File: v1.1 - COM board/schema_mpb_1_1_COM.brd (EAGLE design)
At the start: 72.2 x 75.2 mm, 4 parts, among them IC1 E73_2G4M04S, U1 ESP-WROOM-32

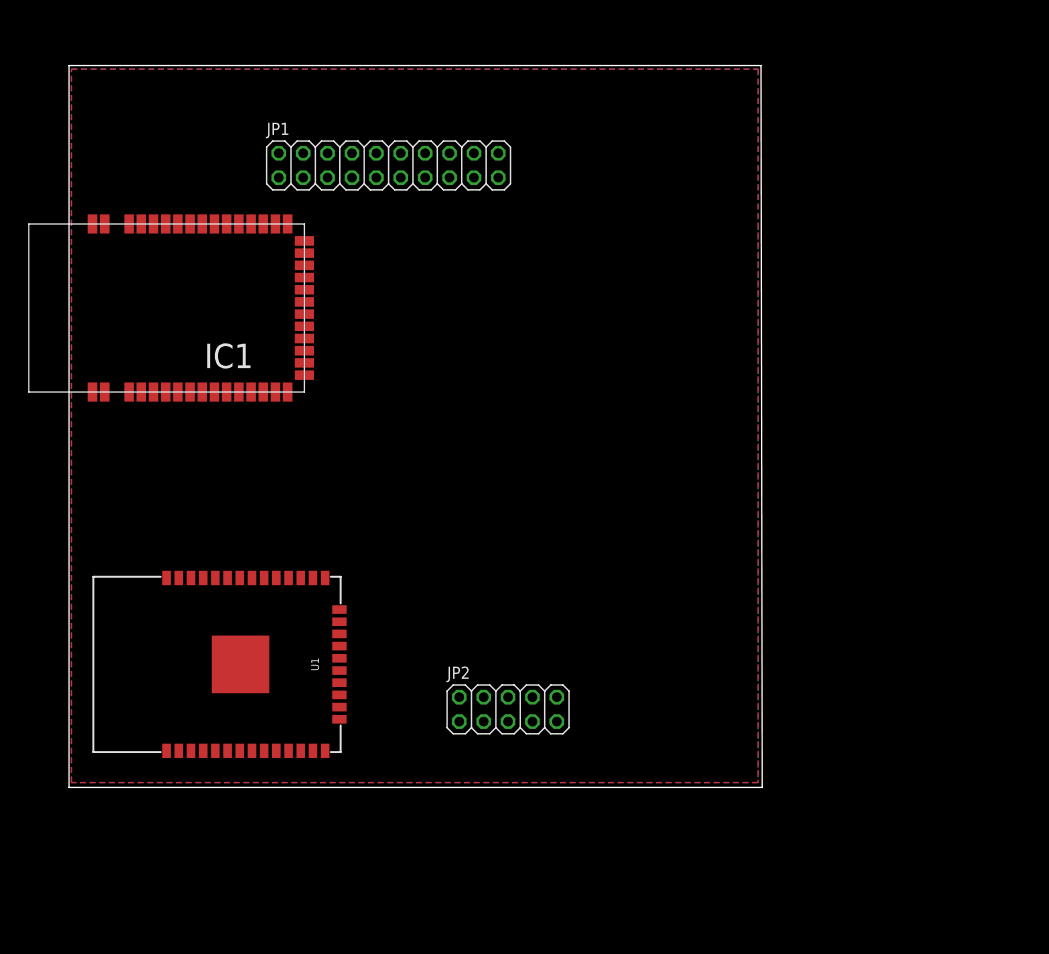
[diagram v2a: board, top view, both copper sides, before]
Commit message: COM board
- Routed first version of Wireless COM board
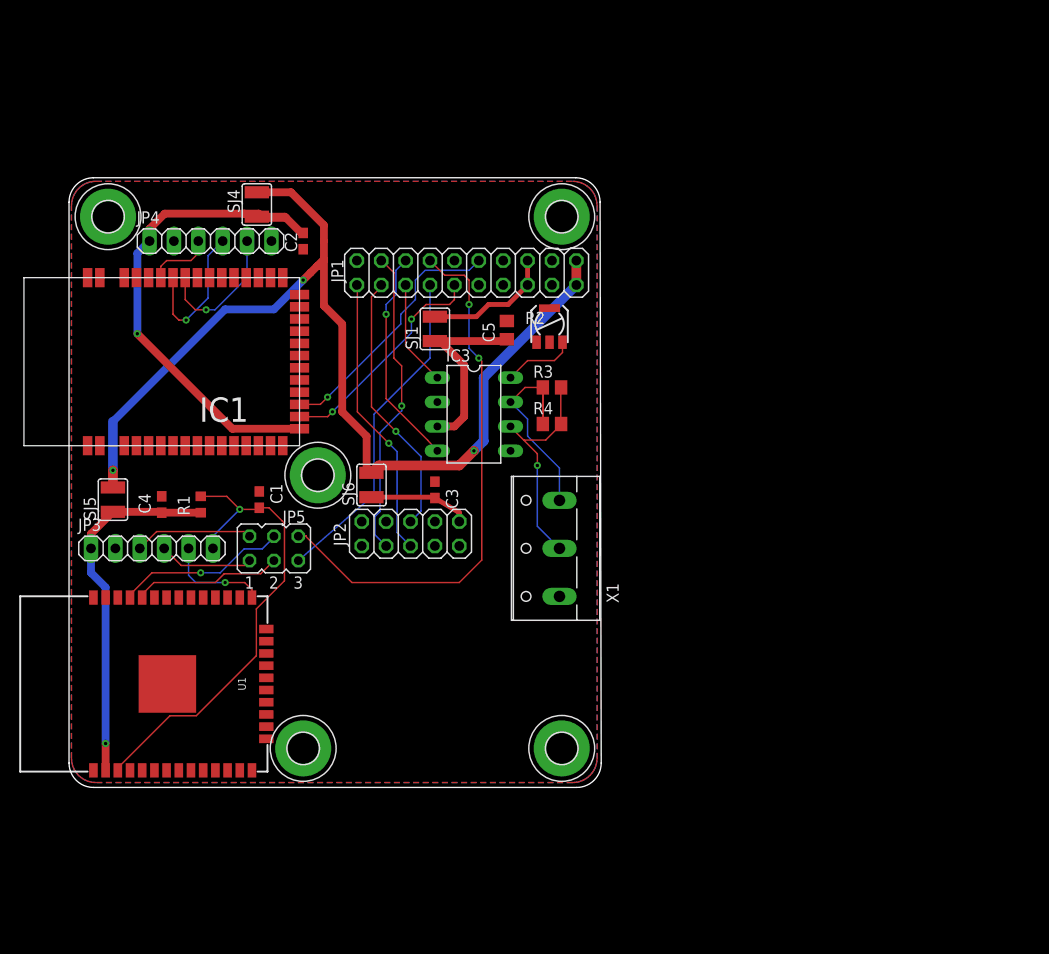
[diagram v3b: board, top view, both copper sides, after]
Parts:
- added C1, C2, C4: .1uF, resistor:C0603
- added C3: (no value), resistor:C0603
- added C5: 0.1uF, resistor:C0805
- added H1, H2, H3, H4, H5: MOUNT-PAD-ROUND3.2, holes:3,2-PAD
- added IC3: PCA82C250, micro-philips:DIL08
- added JP3, JP4: (no value), pinhead:1X06
- added JP5: (no value), jumper:JP3Q
- added R1: 10K, resistor:R0603
- added R2: 25K to 200K, pot-vitrohm:PC25
- added R3, R4: 120, resistor:R0805
- added SJ1, SJ4, SJ5, SJ6: (no value), jumper:SJW
- added X1: (no value), con-wago-500:W237-103
- moved JP2 20.9 mm to (35.6, 26.4), turned to 180 degrees
- moved JP1 13.8 mm to (41.4, 53.6)
- moved U1 7.89 mm to (10.2, 10.8)
- moved IC1 5.61 mm to (24.0, 53.1)
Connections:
- net NRF_IRQ renamed PB8
- net NRF_MISO renamed PB4
- removed net N$10: IC1.36
- removed net N$2: U1.2
- removed net N$3: U1.35
- removed net N$4: U1.34
- removed net N$5: U1.15
- removed net N$6: IC1.0, IC1.1, IC1.15, IC1.2, IC1.42, IC1.43
- removed net N$8: IC1.37
- removed net N$9: IC1.16
- removed net NRF_CE: JP1.9
- removed net NRF_CS: JP1.12
- removed net NRF_MOSI: JP1.7
- removed net NRF_SCK: JP1.8
- new net CANH: IC3.7, R3.2, R4.2, X1.3
- new net CANL: IC3.6, R3.1, R4.1, X1.2
- new net ESP_EN: C1.2, JP3.6, R1.2, U1.3
- new net ESP_IO0: JP3.5, U1.25
- new net ESP_RX: JP1.7, JP5.5
- new net ESP_RX#: JP3.4, JP5.1
- new net ESP_RXD: JP5.3, U1.34
- new net ESP_TX: JP1.8, JP5.6
- new net ESP_TX#: JP3.3, JP5.2
- new net ESP_TXD: JP5.4, U1.35
- new net ETH_CLK: JP2.9
- new net ETH_CS: JP2.3
- new net ETH_NT: JP2.10
- new net ETH_RST: JP2.4
- new net N$12: U1.20
- new net NRF_RST: IC1.36, JP4.5
- new net NRF_RX: IC1.18, JP1.12
- new net NRF_SWDCLK: IC1.37, JP4.4
- new net NRF_SWDIO: IC1.38, JP4.3
- new net NRF_TX: IC1.17, JP1.9
- new net VCC_CAN: C5.1, IC3.3, SJ1.1
- new net VCC_ESP: C4.2, JP3.1, R1.1, SJ5.1, U1.2
- new net VCC_ETH: C3.2, JP2.1, SJ6.1
- new net VCC_NRF: C2.2, IC1.16, JP4.1, SJ4.1
- new net WOL: JP2.7
- net +3.3V: now also SJ4.2, SJ5.2, SJ6.2
- net +5V: now also SJ1.2
- net CAN1_RX: now also IC3.1
- net CAN1_TX: now also IC3.4
- net ETH_MISO: now also JP2.8
- net ETH_MOSI: now also JP2.5
- net ETH_SCK: now also JP2.6
- net GND: now also C1.1, C2.1, C3.1, C4.1, C5.2, IC1.0, IC1.1, IC1.15, IC1.2, IC1.42, IC1.43, IC3.2, JP2.2, JP3.2, JP4.2, R2.A, U1.1, U1.15, U1.38, X1.1
- net N$1: now also IC3.8, R2.E; no longer U1.1
- net N$7: now also JP4.6; no longer IC1.38
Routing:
- net +3.3V: track 0.00 -> 108.8 mm, vias 0 -> 3
- net ESP_TX: track 0.00 -> 56.8 mm, vias 0 -> 2
- net VCC_NRF: track 0.00 -> 54.5 mm, vias 0 -> 1
- net ESP_EN: track 0.00 -> 49.9 mm, vias 0 -> 1
- net VCC_ESP: track 0.00 -> 37.7 mm, vias 0 -> 1
- net ESP_RX: track 0.00 -> 34.7 mm
- net ETH_MISO: track 0.00 -> 32.3 mm, vias 0 -> 1
- net ETH_SCK: track 0.00 -> 29.5 mm, vias 0 -> 1
- net ETH_MOSI: track 0.00 -> 27.7 mm, vias 0 -> 1
- net NRF_RX: track 0.00 -> 26.7 mm, vias 0 -> 1
- net CANH: track 0.00 -> 24.2 mm
- net CANL: track 0.00 -> 23.6 mm, vias 0 -> 1
- net NRF_TX: track 0.00 -> 23.5 mm, vias 0 -> 2
- net CAN1_TX: track 0.00 -> 22.8 mm, vias 0 -> 1
- net VCC_CAN: track 0.00 -> 21.1 mm
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- added copper zone on layer 1, net GND
- added copper zone on layer 16, net GND
- removed copper zone on layer 16, net N$11
- removed copper zone on layer 1, net N$14
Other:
- board size 72.2 x 75.2 mm -> 55.4 x 63.5 mm

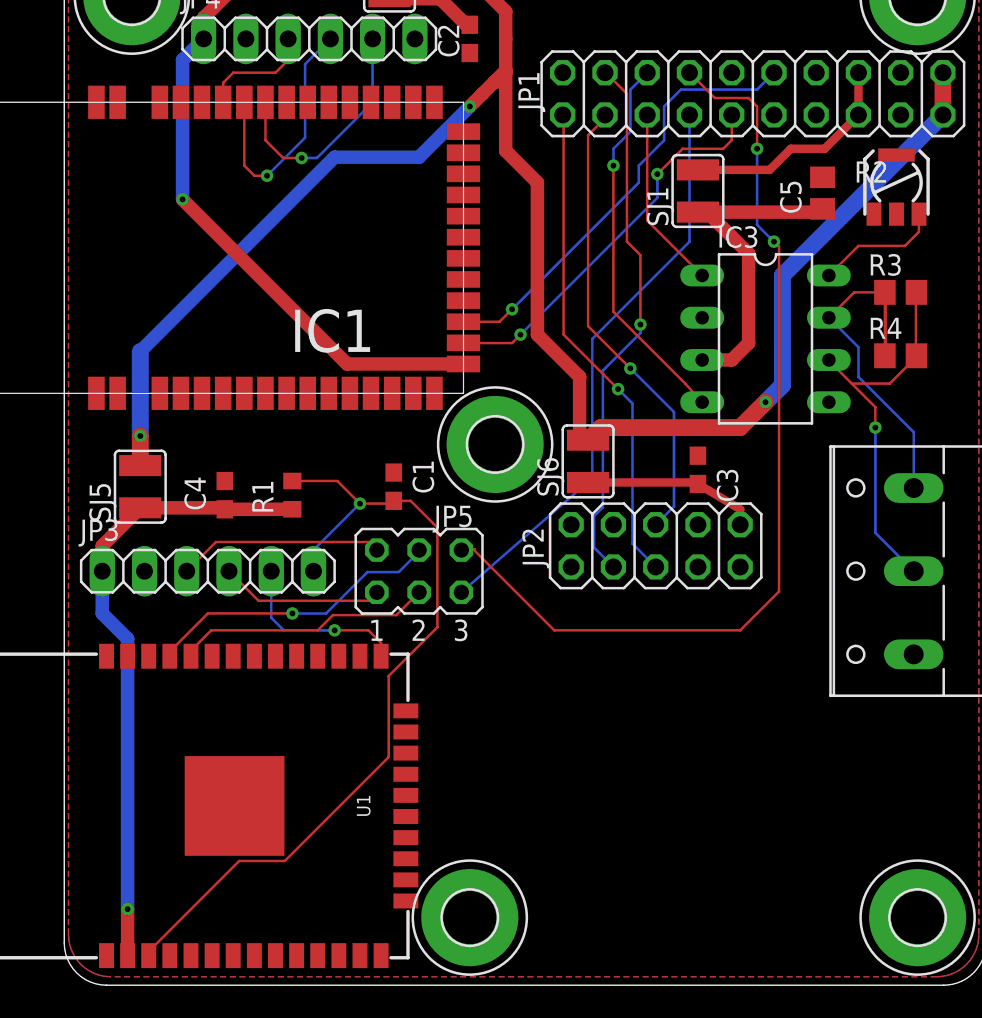
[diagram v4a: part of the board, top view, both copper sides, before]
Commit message: Wireless board
- Changed drill sizes, got rid of via clearance issues
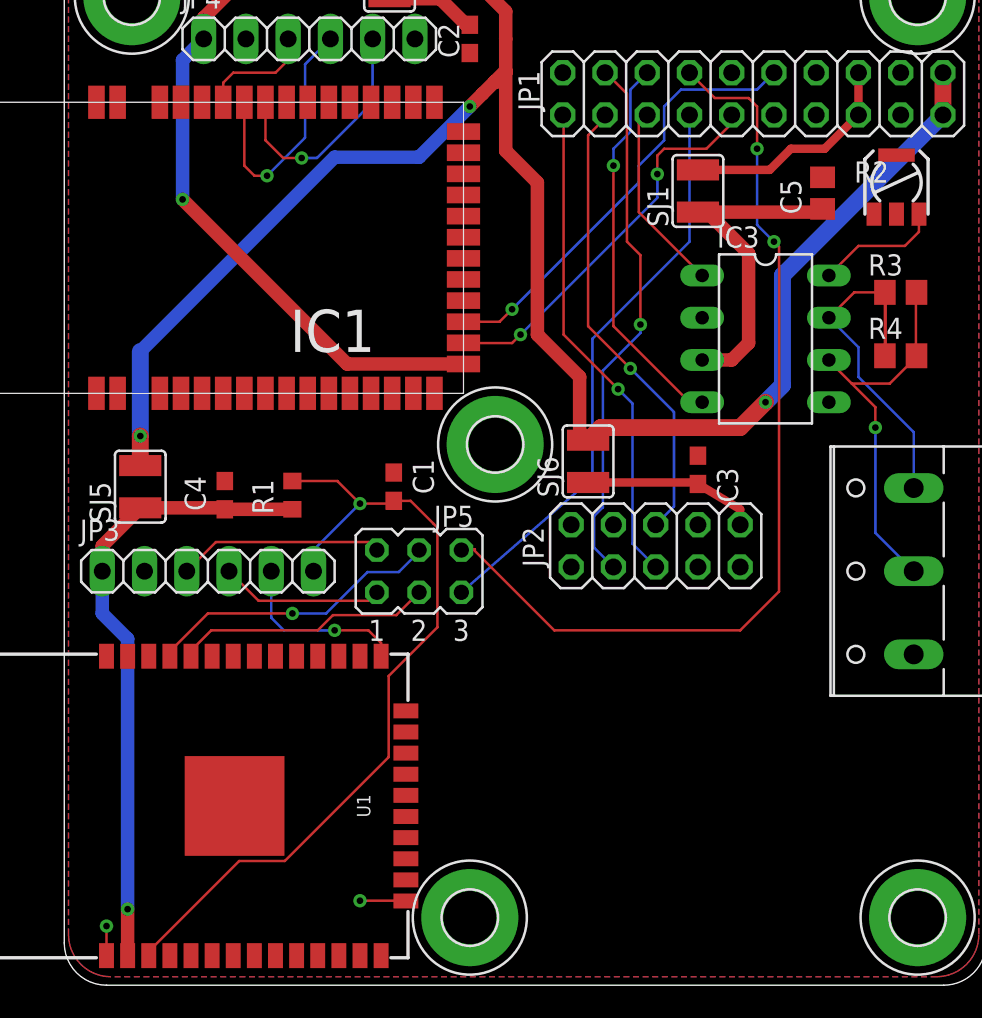
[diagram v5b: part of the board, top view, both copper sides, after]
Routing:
- net GND: track 0.00 -> 4.55 mm, vias 0 -> 2

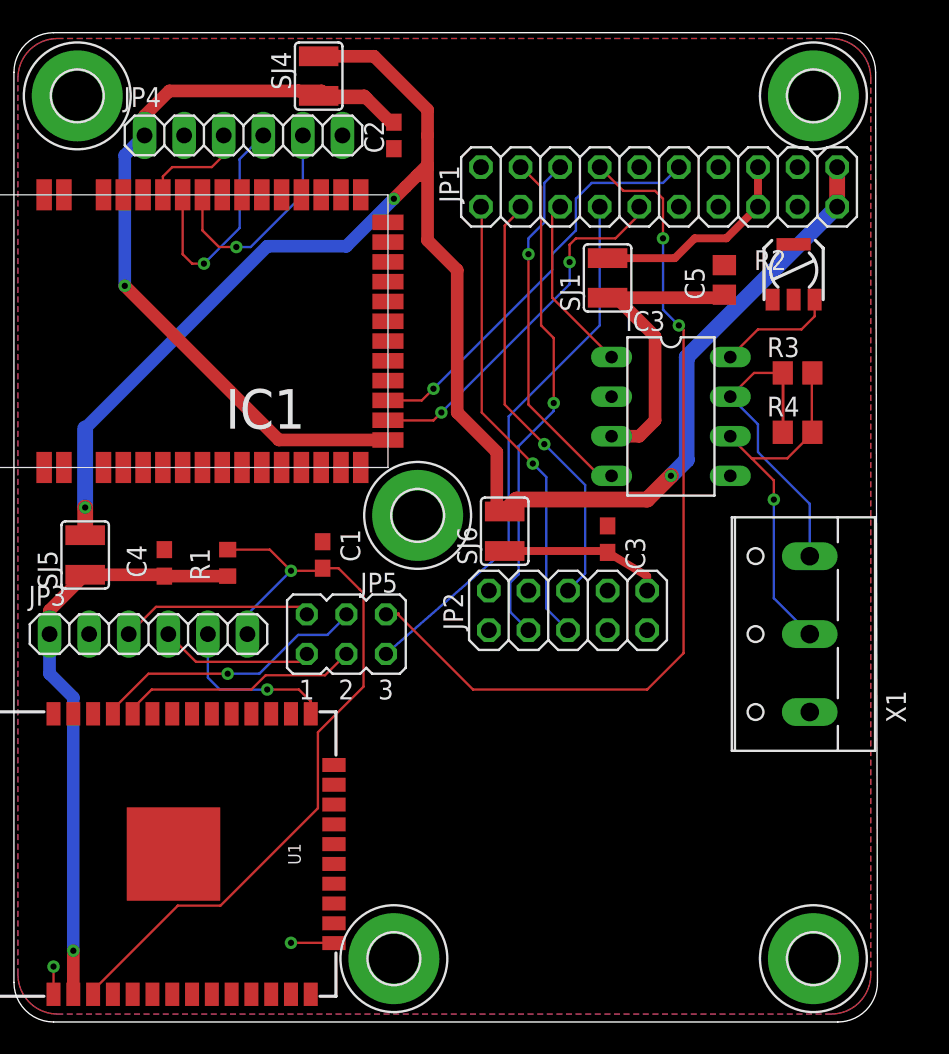
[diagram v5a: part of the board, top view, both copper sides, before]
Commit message: COM revision
- Added Ethernet module outline
- Adjusted track width
- labelled CAN terminals
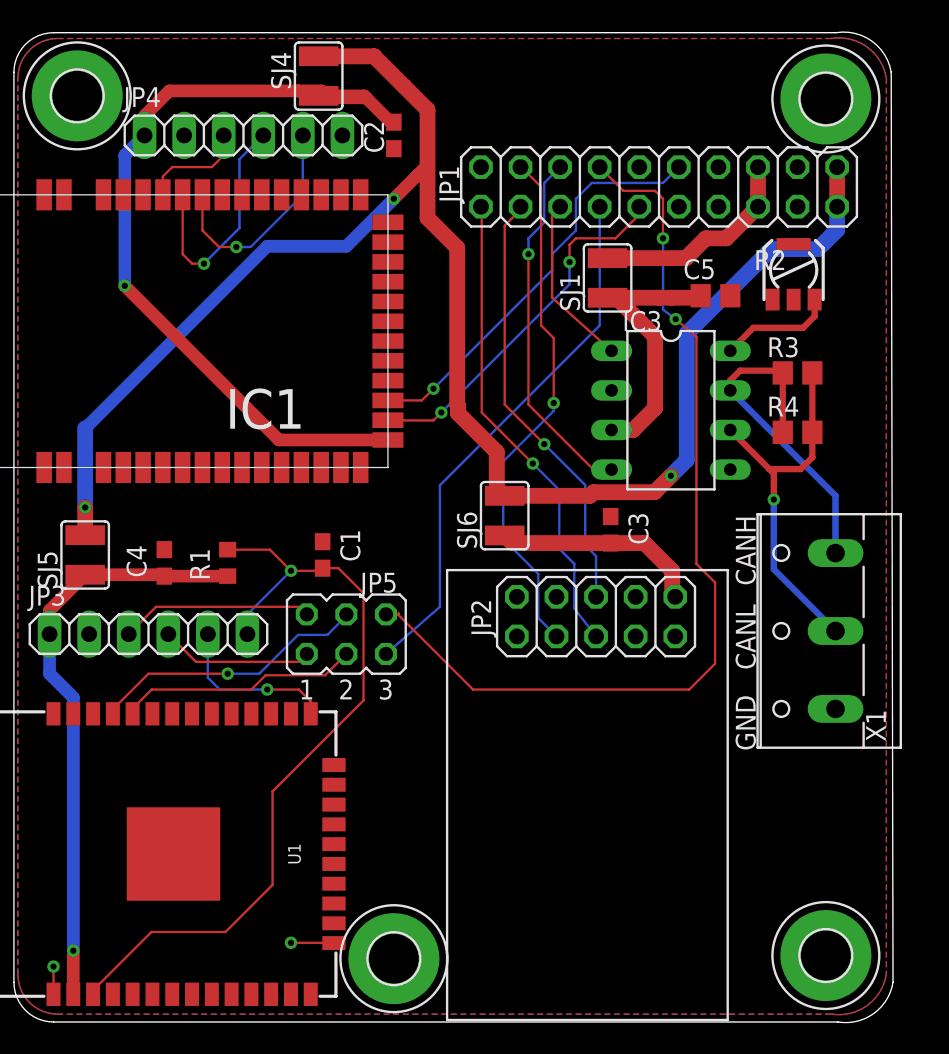
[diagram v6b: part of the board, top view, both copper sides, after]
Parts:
- removed H5: MOUNT-PAD-ROUND3.2, holes:3,2-PAD
- moved JP2 1.84 mm to (37.4, 26.0)
- moved X1 1.67 mm to (51.4, 25.1)
- moved C5 1.17 mm to (45.0, 46.6), turned to 0 degrees
- moved SJ6 1.00 mm to (31.5, 32.5)
- moved H2 0.82 mm to (52.1, 59.2)
- moved H3 0.82 mm to (52.1, 4.26)
- moved C3 0.63 mm to (38.3, 31.6)
- moved IC3 0.40 mm to (42.2, 39.3)
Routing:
- net +3.3V: track 108.8 -> 118.8 mm
- net CANL: track 23.6 -> 28.2 mm
- net VCC_ETH: track 17.6 -> 13.4 mm
- net ESP_TX: track 56.8 -> 60.2 mm
- net VCC_CAN: track 21.1 -> 18.7 mm
- net ETH_MISO: track 32.3 -> 33.8 mm
- net ESP_EN: track 49.9 -> 51.1 mm
- net CANH: track 24.2 -> 25.3 mm
- net ETH_SCK: track 29.5 -> 30.5 mm
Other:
- board size 55.4 x 63.5 mm -> 56.4 x 63.6 mm
- board text added: "CANH"
- board text added: "CANL"
- board text added: "GND"
